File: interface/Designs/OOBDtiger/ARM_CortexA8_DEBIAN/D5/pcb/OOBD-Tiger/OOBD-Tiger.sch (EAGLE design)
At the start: 112 parts, among them IC1 ADM3053M, IC2 ADM3053M, IC4 DS3231, U1 SY6280, U10 MP1482DS, U2 SN65HVD230(SO8), U3 SY6280, U6 SN65HVD230(SO8)

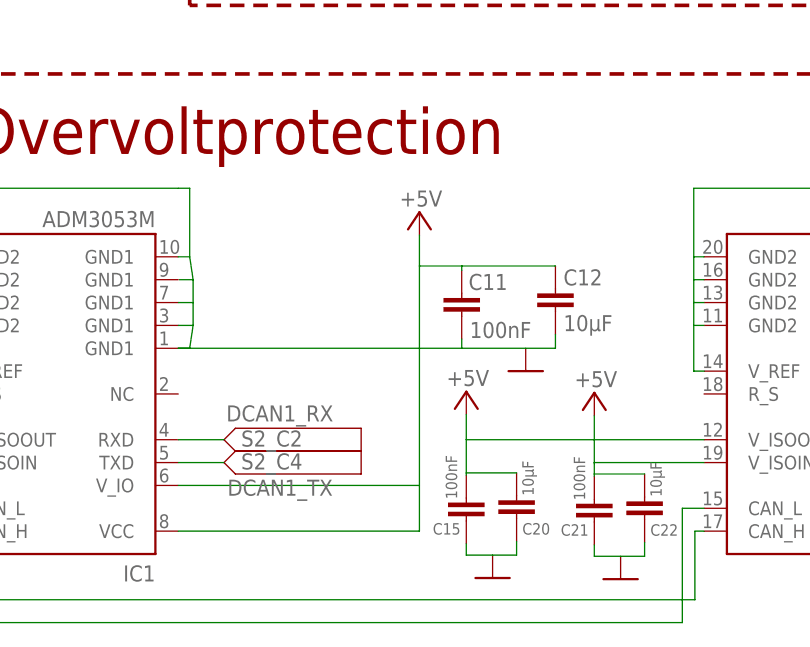
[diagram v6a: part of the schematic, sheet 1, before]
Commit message: Erster adm3053 Plazierungsversuch, Kondensatoren nahe an IC, aber nicht so nah wie in der Alpnote.
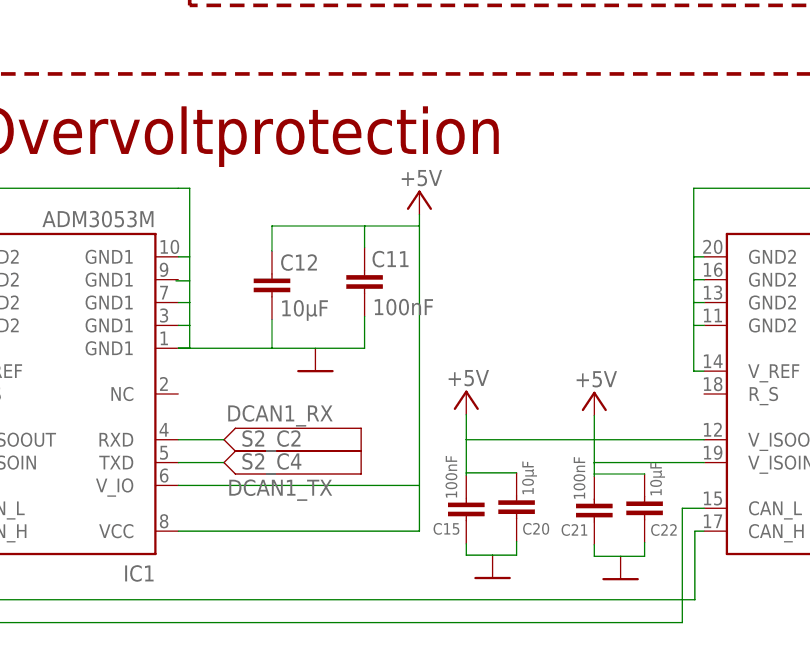
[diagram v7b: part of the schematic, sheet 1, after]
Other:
- moved on the sheet: C11, C12
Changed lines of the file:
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@@
 <attribute name="VALUE" x="17.78" y="100.965" size="1.778" layer="96"/>
 </instance>
-<instance part="GND34" gate="1" x="160.528" y="45.72"/>
+<instance part="GND34" gate="1" x="137.16" y="45.72"/>
 <instance part="GND36" gate="1" x="240.919" y="45.72"/>
-<instance part="P+8" gate="1" x="148.717" y="63.373" smashed="yes" rot="MR0">
-<attribute name="VALUE" x="151.257" y="64.008" size="1.778" layer="96" rot="MR0"/>
+<instance part="P+8" gate="1" x="148.717" y="65.659" smashed="yes" rot="MR0">
+<attribute name="VALUE" x="151.257" y="66.294" size="1.778" layer="96" rot="MR0"/>
 </instance>
 <instance part="P+9" gate="1" x="236.474" y="66.167" smashed="yes" rot="MR0">
 <attribute name="VALUE" x="239.014" y="66.802" size="1.778" layer="96" rot="MR0"/>
 </instance>
-<instance part="C11" gate="G$1" x="153.416" y="54.356" smashed="yes">
-<attribute name="NAME" x="154.178" y="54.737" size="1.778" layer="95"/>
-<attribute name="VALUE" x="154.305" y="49.403" size="1.778" layer="96"/>
-</instance>
-<instance part="C12" gate="G$1" x="163.83" y="54.864" smashed="yes">
-<attribute name="NAME" x="164.719" y="55.245" size="1.778" layer="95"/>
-<attribute name="VALUE" x="164.719" y="50.165" size="1.778" layer="96"/>
+<instance part="C11" gate="G$1" x="142.621" y="56.896" smashed="yes">
+<attribute name="NAME" x="143.383" y="57.277" size="1.778" layer="95"/>
+<attribute name="VALUE" x="143.51" y="51.943" size="1.778" layer="96"/>
+</instance>
+<instance part="C12" gate="G$1" x="132.334" y="56.515" smashed="yes">
+<attribute name="NAME" x="133.223" y="56.896" size="1.778" layer="95"/>
+<attribute name="VALUE" x="133.223" y="51.816" size="1.778" layer="96"/>
 </instance>
 <instance part="C13" gate="G$1" x="229.108" y="55.372" smashed="yes">
@@
 <pinref part="IC1" gate="G$1" pin="GND1@0"/>
 <pinref part="GND34" gate="1" pin="GND"/>
-<wire x1="121.92" y1="48.26" x2="153.416" y2="48.26" width="0.1524" layer="91"/>
-<wire x1="153.416" y1="48.26" x2="160.528" y2="48.26" width="0.1524" layer="91"/>
+<wire x1="121.92" y1="48.26" x2="132.334" y2="48.26" width="0.1524" layer="91"/>
+<wire x1="142.621" y1="48.26" x2="137.16" y2="48.26" width="0.1524" layer="91"/>
 <pinref part="IC1" gate="G$1" pin="GND1@1"/>
-<wire x1="123.19" y1="58.42" x2="123.571" y2="55.88" width="0.1524" layer="91"/>
-<wire x1="123.571" y1="55.88" x2="123.571" y2="53.34" width="0.1524" layer="91"/>
-<wire x1="123.571" y1="53.34" x2="123.571" y2="50.8" width="0.1524" layer="91"/>
-<wire x1="121.92" y1="50.8" x2="123.571" y2="50.8" width="0.1524" layer="91"/>
-<wire x1="123.571" y1="50.8" x2="123.19" y2="48.26" width="0.1524" layer="91"/>
+<wire x1="123.19" y1="58.42" x2="123.19" y2="55.753" width="0.1524" layer="91"/>
+<wire x1="123.19" y1="55.753" x2="123.19" y2="53.34" width="0.1524" layer="91"/>
+<wire x1="123.19" y1="53.34" x2="123.19" y2="50.8" width="0.1524" layer="91"/>
+<wire x1="121.92" y1="50.8" x2="123.19" y2="50.8" width="0.1524" layer="91"/>
+<wire x1="123.19" y1="50.8" x2="123.19" y2="48.26" width="0.1524" layer="91"/>
 <wire x1="123.19" y1="48.26" x2="121.92" y2="48.26" width="0.1524" layer="91"/>
 <pinref part="C11" gate="G$1" pin="2"/>
-<wire x1="153.416" y1="49.276" x2="153.416" y2="48.26" width="0.1524" layer="91"/>
+<wire x1="142.621" y1="51.816" x2="142.621" y2="48.26" width="0.1524" layer="91"/>
 <pinref part="C12" gate="G$1" pin="2"/>
-<wire x1="163.83" y1="49.784" x2="163.83" y2="48.26" width="0.1524" layer="91"/>
-<wire x1="163.83" y1="48.26" x2="160.528" y2="48.26" width="0.1524" layer="91"/>
-<wire x1="122.047" y1="55.88" x2="123.571" y2="55.88" width="0.1524" layer="91"/>
+<wire x1="132.334" y1="51.435" x2="132.334" y2="48.26" width="0.1524" layer="91"/>
+<wire x1="132.334" y1="48.26" x2="137.16" y2="48.26" width="0.1524" layer="91"/>
+<wire x1="121.666" y1="55.753" x2="123.19" y2="55.753" width="0.1524" layer="91"/>
 <pinref part="IC1" gate="G$1" pin="GND1@2"/>
-<wire x1="121.92" y1="53.34" x2="123.571" y2="53.34" width="0.1524" layer="91"/>
+<wire x1="121.92" y1="53.34" x2="123.19" y2="53.34" width="0.1524" layer="91"/>
 </segment>
 <segment>
@@
 <segment>
 <pinref part="C12" gate="G$1" pin="1"/>
-<wire x1="153.416" y1="57.404" x2="163.83" y2="57.404" width="0.1524" layer="91"/>
+<wire x1="132.334" y1="61.849" x2="132.334" y2="59.055" width="0.1524" layer="91"/>
 <pinref part="C11" gate="G$1" pin="1"/>
-<wire x1="153.416" y1="56.896" x2="153.416" y2="57.404" width="0.1524" layer="91"/>
+<wire x1="142.621" y1="59.436" x2="142.621" y2="61.849" width="0.1524" layer="91"/>
+<wire x1="142.621" y1="61.849" x2="132.334" y2="61.849" width="0.1524" layer="91"/>
 <pinref part="P+8" gate="1" pin="+5V"/>
-<wire x1="148.717" y1="60.833" x2="148.717" y2="57.404" width="0.1524" layer="91"/>
-<wire x1="148.717" y1="57.404" x2="153.416" y2="57.404" width="0.1524" layer="91"/>
+<wire x1="148.717" y1="63.119" x2="148.717" y2="61.849" width="0.1524" layer="91"/>
+<wire x1="148.717" y1="61.849" x2="142.621" y2="61.849" width="0.1524" layer="91"/>
 <pinref part="IC1" gate="G$1" pin="VCC"/>
-<wire x1="148.717" y1="57.404" x2="148.717" y2="33.02" width="0.1524" layer="91"/>
+<wire x1="148.717" y1="61.849" x2="148.717" y2="33.02" width="0.1524" layer="91"/>
 <wire x1="148.717" y1="33.02" x2="148.717" y2="27.94" width="0.1524" layer="91"/>
 <wire x1="148.717" y1="27.94" x2="121.92" y2="27.94" width="0.1524" layer="91"/>

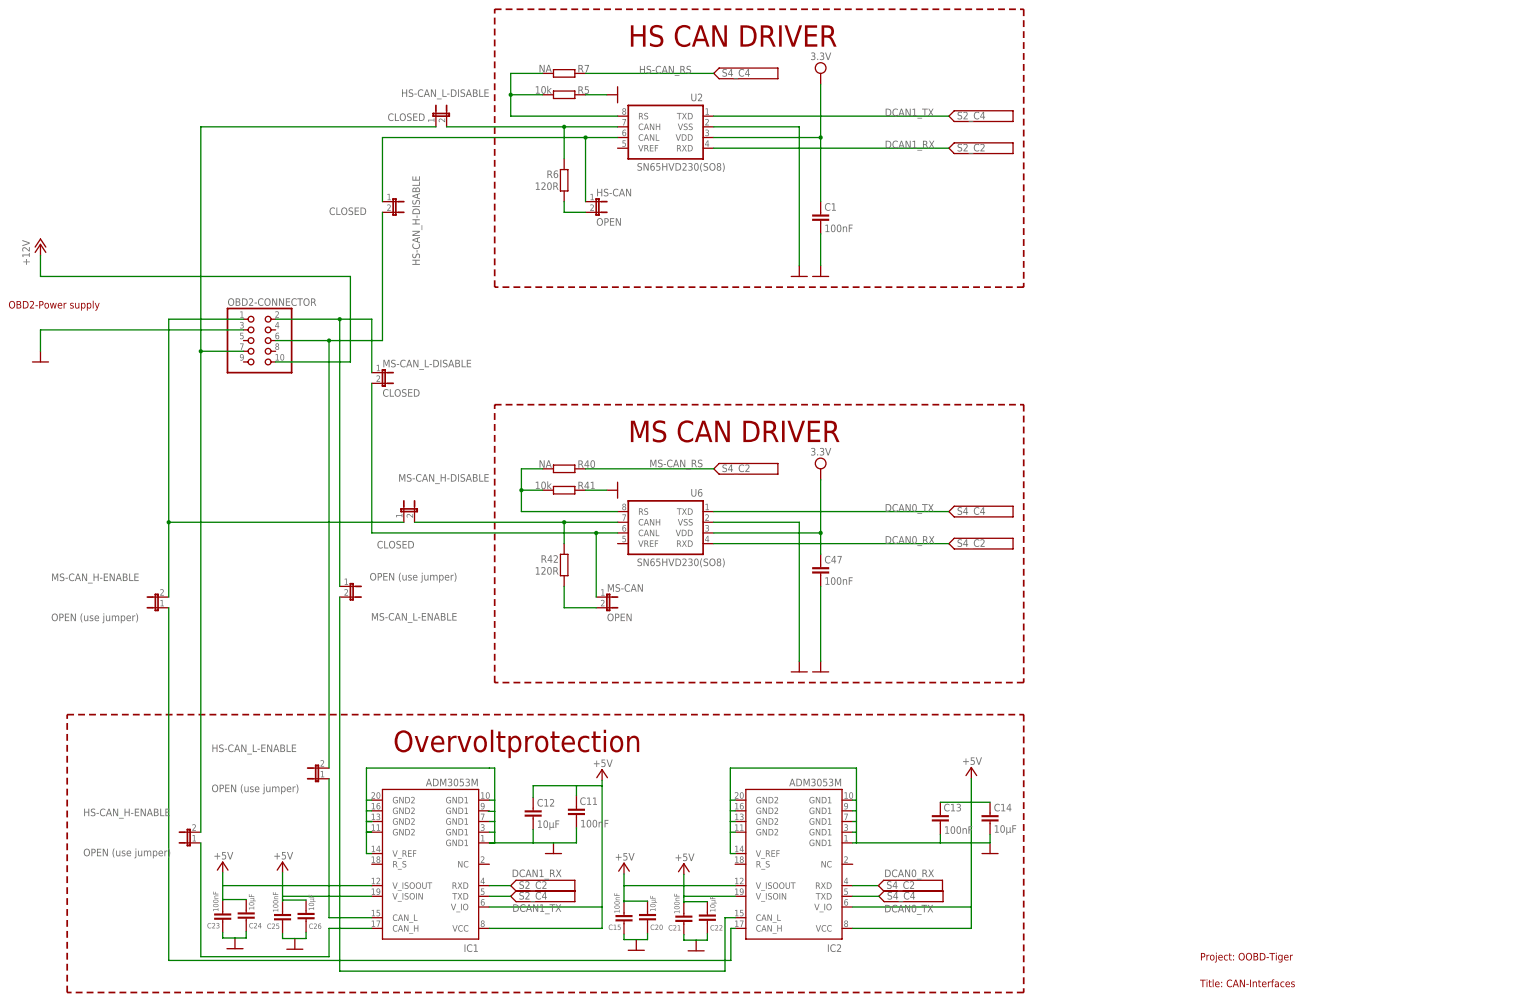
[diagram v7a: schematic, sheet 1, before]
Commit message: fix ERC findings modify and fix ADM3053 connections remove jumper against optional 0R resistors for Standard CAN interface
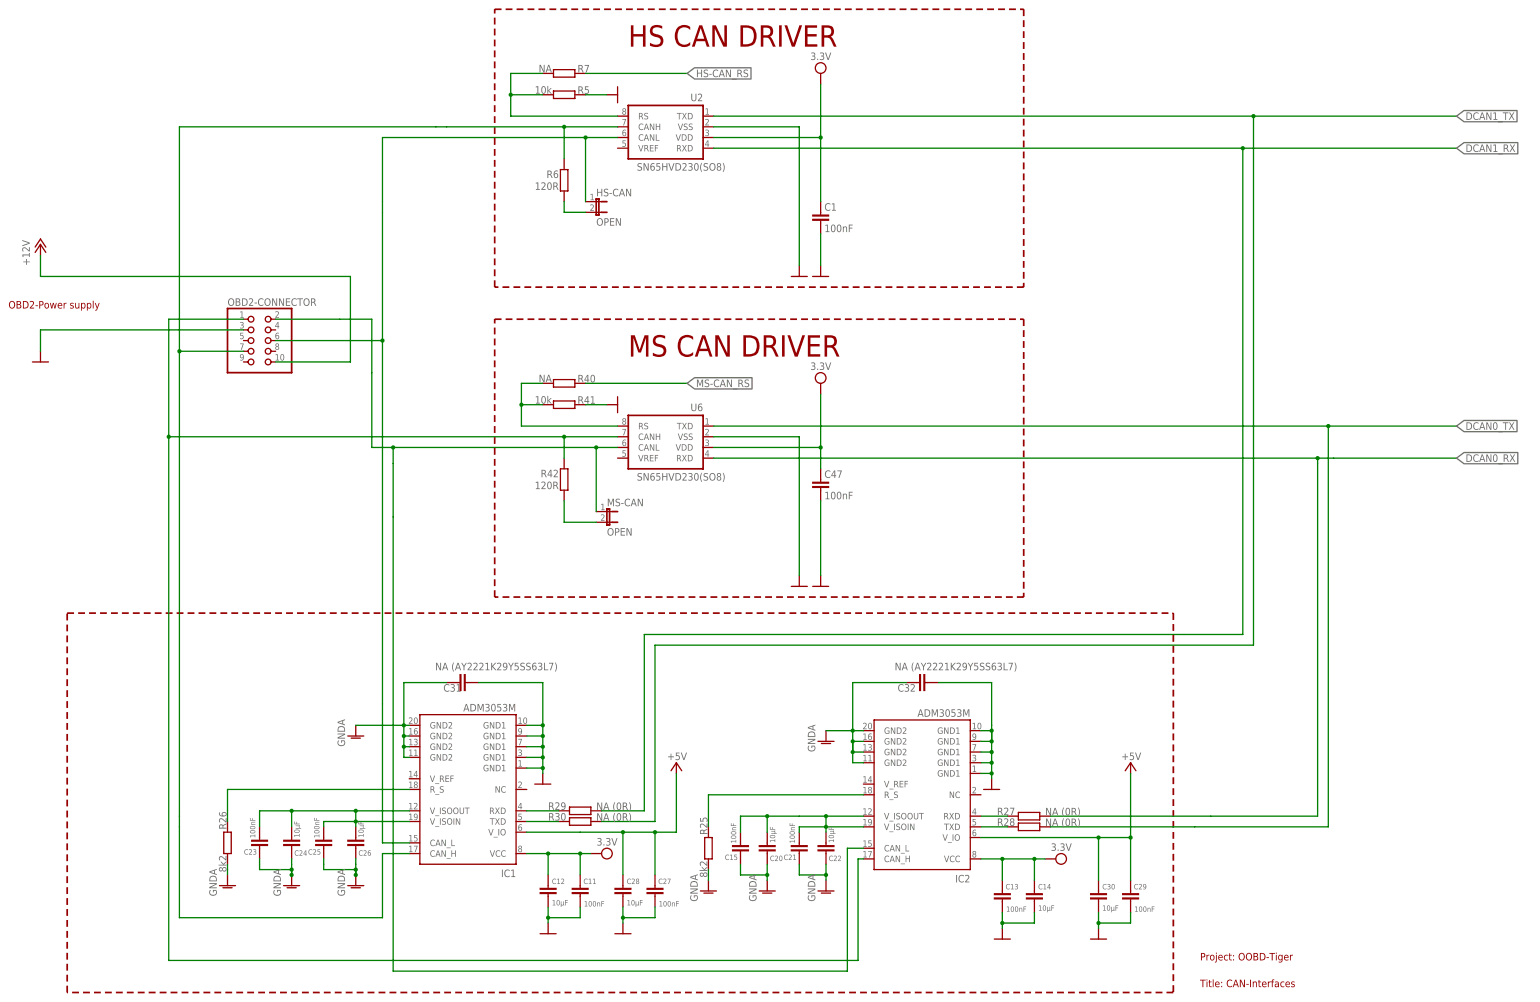
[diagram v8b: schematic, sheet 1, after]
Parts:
- removed HS-CAN_H-DISABLE, HS-CAN_L-DISABLE, MS-CAN_H-DISABLE, MS-CAN_L-DISABLE: CLOSED, SparkFun:JUMPER-2SMD-NO
- removed HS-CAN_H-ENABLE, HS-CAN_L-ENABLE, MS-CAN_H-ENABLE, MS-CAN_L-ENABLE: OPEN (use jumper), SparkFun:JUMPER-2SMD-NO
- added C27, C29: 100nF, rcl:C-EUC0603K
- added C28, C30: 10µF, rcl:C-EUC0805K
- added C31, C32: NA (AY2221K29Y5SS63L7), rcl:C-EU075-032X103
- added R25, R26: 8k2, rcl:R-EU_R0603
- added R27, R28, R29, R30: NA (0R), rcl:R-EU_0207/10
- C1, C47: device rcl:C-EU2 -> rcl:C-EU075-032X103
- C10, C8: device rcl:C-EUC0603_DWS -> rcl:C-EUC0805K
- C11, C13, C15, C21, C23, C25: device rcl:C-EU2 -> rcl:C-EUC0603K
- C12, C14, C20, C22, C24, C26: device rcl:C-EU2 -> rcl:C-EUC0805K
- C2, C4, C6: device rcl:C-EUC0603 -> rcl:C-EUC0603K
- C3: device rcl:C-EUC0603_DWS -> rcl:C-EUC0603K
- C63, C64: device rcl:C-EUC0603 -> rcl:C-EUC0805K
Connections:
- removed net CANH: IC2.CAN_H, MS-CAN_H-ENABLE.1
- removed net CANH1: HS-CAN_H-ENABLE.2, HS-CAN_L-DISABLE.1, OBD2-CONNECTOR.7
- removed net CANL: MS-CAN.1, MS-CAN_L-DISABLE.2, U6.CANL
- removed net CANL1: HS-CAN.1, HS-CAN_H-DISABLE.1, U2.CANL
- removed net N$30: HS-CAN_L-DISABLE.2, R6.2, U2.CANH
- removed net N$32: IC2.CAN_L, MS-CAN_L-ENABLE.2
- removed net N$36: MS-CAN_L-DISABLE.1, MS-CAN_L-ENABLE.1, OBD2-CONNECTOR.2
- removed net N$37: MS-CAN_H-DISABLE.1, MS-CAN_H-ENABLE.2, OBD2-CONNECTOR.1
- removed net N$38: IC2.GND2@0, IC2.GND2@1, IC2.GND2@2, IC2.V_REF
- removed net N$40: IC1.V_ISOIN
- removed net N$42: IC2.GND1@3, IC2.GND1@4, IC2.GND2@3
- removed net N$45: IC1.GND2@0, IC1.GND2@1, IC1.GND2@2, IC1.V_REF
- removed net N$46: IC1.GND1@4, IC1.GND2@3
- removed net VCC: AM3352-SOM-EVB-PLATFORM.3.3V@3, AM3352-SOM-EVB-PLATFORM.3.3V@4, C1.1, C47.1, R47.2, U2.VDD, U6.VDD
- new net 3V3: AM3352-SOM-EVB-PLATFORM.3.3V@3, AM3352-SOM-EVB-PLATFORM.3.3V@4, C1.1, C11.1, C12.1, C13.1, C14.1, C47.1, IC1.VCC, IC2.VCC, R47.2, U2.VDD, U6.VDD
- new net CAN0_H: IC2.CAN_H, OBD2-CONNECTOR.1, R42.2, U6.CANH
- new net CAN0_L: IC2.CAN_L, MS-CAN.1, OBD2-CONNECTOR.2, U6.CANL
- new net CAN1_H: IC1.CAN_H, OBD2-CONNECTOR.7, R6.2, U2.CANH
- new net CAN1_L: HS-CAN.1, IC1.CAN_L, OBD2-CONNECTOR.6, U2.CANL
- new net GNDA: C15.2, C20.2, C21.2, C22.2, C23.2, C24.2, C25.2, C26.2, C31.1, C32.1, IC1.GND2@0, IC1.GND2@1, IC1.GND2@2, IC1.GND2@3, IC2.GND2@0, IC2.GND2@1, IC2.GND2@2, IC2.GND2@3, R25.1, R26.1
- new net N$50: C15.1, C20.1, C21.1, C22.1, IC2.V_ISOIN, IC2.V_ISOOUT
- new net N$52: IC1.R_S, R26.2
- net +5V: now also C27.1, C28.1, C29.1, C30.1, IC2.V_IO; no longer C11.1, C12.1, C13.1, C14.1, C15.1, C20.1, C21.1, C22.1, C23.1, C24.1, C25.1, C26.1, IC1.VCC, IC2.VCC, IC2.V_ISOIN, IC2.V_ISOOUT
- net DCAN0_RX: now also R27.2
- net DCAN0_TX: now also R28.2
- net DCAN1_RX: now also R29.2
- net DCAN1_TX: now also R30.2
- net GND: now also C27.2, C28.2, C29.2, C30.2, C31.2, C32.2, IC1.GND1@3, IC1.GND1@4, IC2.GND1@3, IC2.GND1@4; no longer C15.2, C20.2, C21.2, C22.2, C23.2, C24.2, C25.2, C26.2
- net N$31: now also C23.1, C24.1, C25.1, C26.1, IC1.V_ISOIN, IC1.V_ISOOUT; no longer HS-CAN_H-DISABLE.2, HS-CAN_L-ENABLE.2, OBD2-CONNECTOR.6
- net N$33: now also IC2.R_S, R25.2; no longer MS-CAN_H-DISABLE.2, R42.2, U6.CANH
- net N$34: now also IC2.RXD, R27.1; no longer HS-CAN_H-ENABLE.1, IC1.CAN_H
- net N$35: now also IC2.TXD, R28.1; no longer HS-CAN_L-ENABLE.1, IC1.CAN_L
- net N$39: now also IC1.RXD, R29.1; no longer IC2.V_IO
- net N$41: now also IC1.TXD, R30.1; no longer IC1.V_ISOOUT
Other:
- note removed: "Overvoltprotection"
- moved on the sheet: C11, C12, C13, C14, C15, C20, C21, C22, C23, C24, C25, C26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
